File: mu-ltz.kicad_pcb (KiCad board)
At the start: 2 copper layers, 34.5 x 60 mm, 47 parts, among them J10 TRIM2, J2 GND, J3 Hi, J5 Lo, J6 Vin+, J9 TRIM1, Q1 MMBT3904LT1G, U1 LTZ1000, U2 AD8667, U3 ADA4523-1

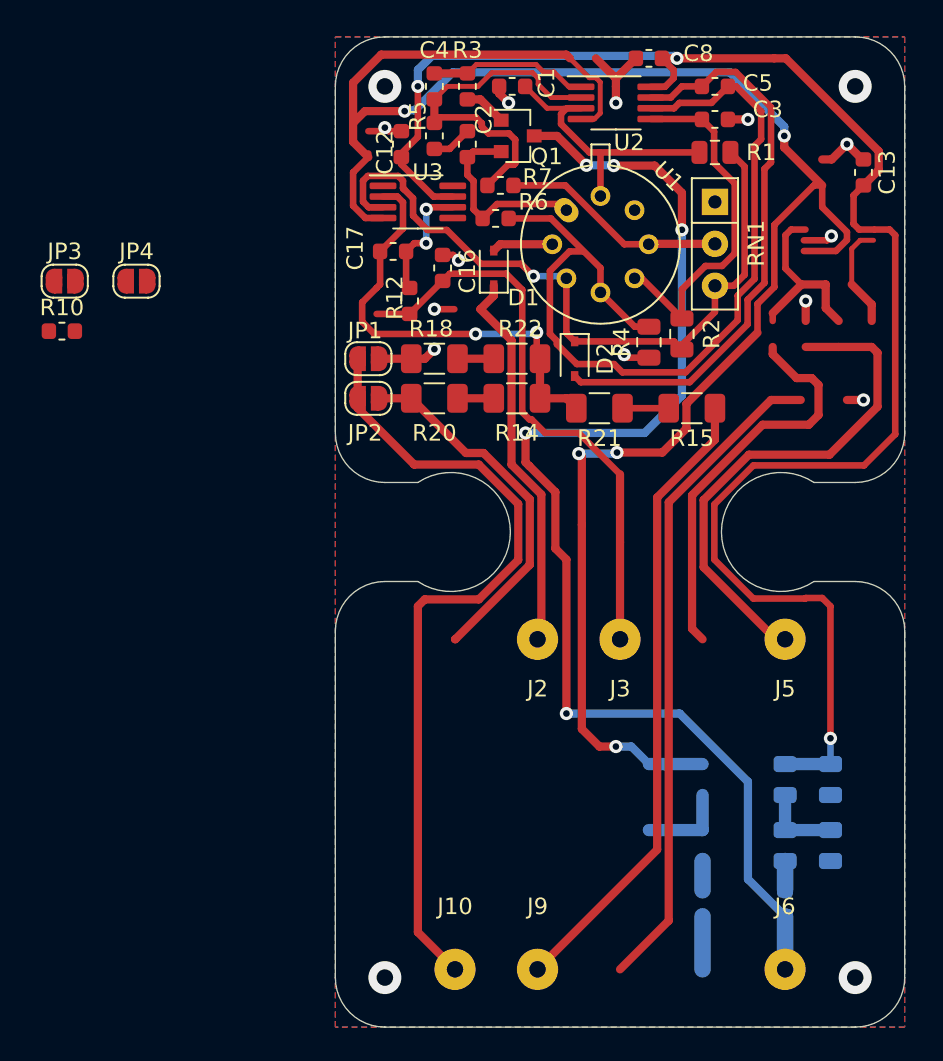
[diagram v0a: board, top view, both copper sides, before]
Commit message: Rev. 0.2 layout finished, not yet tested
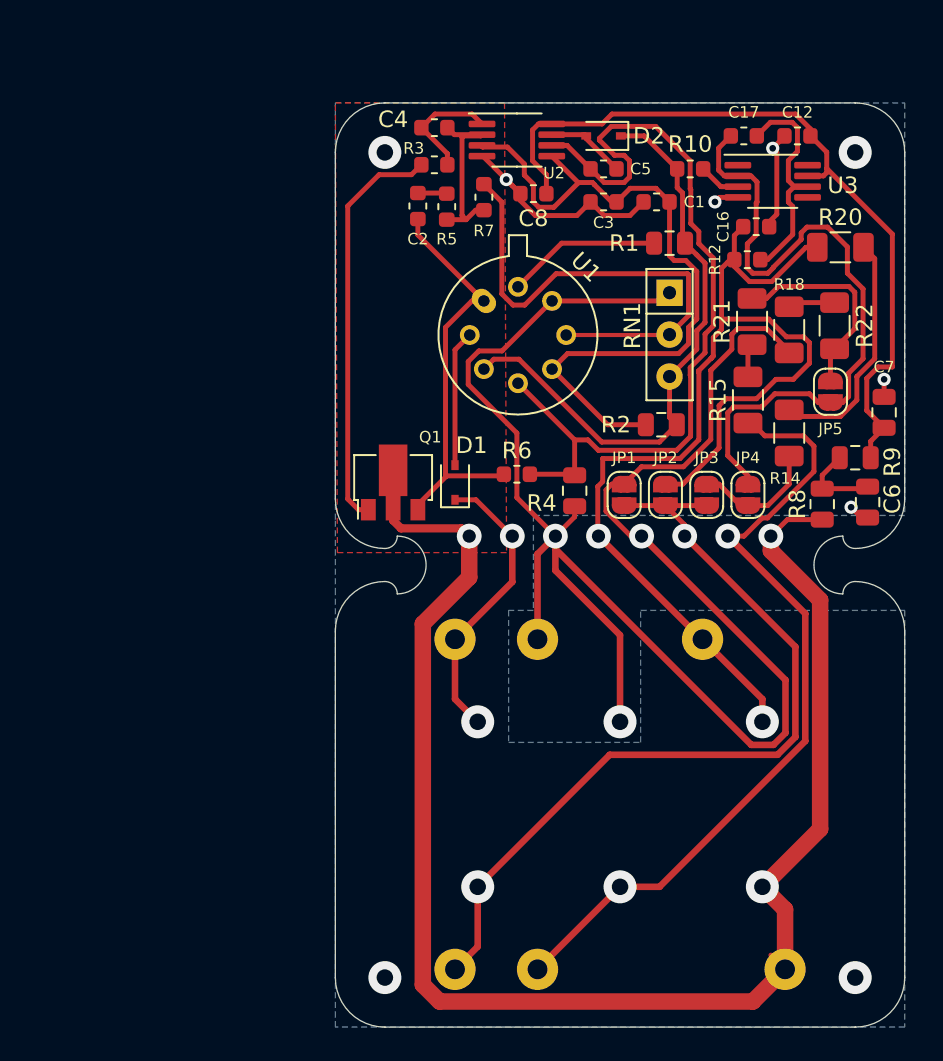
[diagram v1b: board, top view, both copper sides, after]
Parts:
- removed C13: 100nF, Capacitor_SMD:C_0603_1608Metric
- removed FB2: Ferrite_Bead_Small, Inductor_SMD:L_0603_1608Metric
- added JP3: Jumper_NO_Small, Jumper:SolderJumper-2_P1.3mm_Open_RoundedPad1.0x1.5mm, F.Cu at (122.5, 67.8)
- C6, C7, R8, R9: moved to F.Cu
- Q1: value MMBT3904LT1G -> 2SD1628G-TD-E; footprint Package_TO_SOT_SMD:SOT-23 -> Package_TO_SOT_SMD:SOT-89-3
- R6: value 400k -> dnp
- RN1: value 13k 1k -> 13k1k
- moved JP4 43.4 mm to (125.0, 67.8), turned to 270 degrees
- moved JP5 42.6 mm to (130.0, 61.5), turned to 90 degrees
- moved R10 39.3 mm to (121.5, 48.0), turned to 180 degrees
- moved R20 26.2 mm to (130.6, 52.8)
- moved C12 24.0 mm to (128.0, 46.0), turned to 0 degrees
- moved C7 22.5 mm to (133.2, 62.8), turned to 270 degrees
- moved C17 22.4 mm to (124.8, 46.0)
- moved Q1 22.3 mm to (103.5, 67.0), turned to 90 degrees
- moved R18 21.6 mm to (127.5, 57.8), turned to 90 degrees
- moved U3 21.5 mm to (126.5, 48.8)
- moved C6 20.9 mm to (132.2, 68.2)
- moved R8 20.8 mm to (129.5, 68.3)
- moved R12 20.6 mm to (125.0, 53.5), turned to 0 degrees
- moved R9 20.0 mm to (131.5, 65.5), turned to 180 degrees
- moved R22 19.4 mm to (130.2, 57.5), turned to 270 degrees
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- renumbered J2 to J1, J5 to J2, J3 to J4, JP3 to JP4, JP4 to JP5
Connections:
- D1 pad 1: Net-(D1-Pad1) -> /GND
- J1 pad 1: Net-(D1-Pad1) -> /GND
- J2 pad 1: Net-(D1-Pad1) -> /GND
- JP1 pad 1: Net-(D1-Pad1) -> /GND
- JP4 pad 2: Net-(J10-Pad1) -> Net-(JP3-Pad2)
- Q1 pad 2: Net-(C2-Pad2) -> /VCC
- Q1 pad 3: /VCC -> Net-(C2-Pad2)
- R14 pad 2: Net-(C17-Pad1) -> Net-(JP3-Pad2)
- R18 pad 1: Net-(D1-Pad1) -> /GND
- R4 pad 1: Net-(D1-Pad1) -> /GND
- R8 pad 2: Net-(FB2-Pad2) -> /VCC
- RN1 pad 1: Net-(D1-Pad1) -> /GND
- U1 pad 3: Net-(R10-Pad1) -> Net-(D2-Pad1)
- U1 pad 7: Net-(D1-Pad1) -> /GND
- U3 pad 3: Net-(D2-Pad1) -> Net-(R10-Pad1)
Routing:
- net Net-(D1-Pad1): track 60.4 -> 0.00 mm, vias 2 -> 0
- net /V+_filtered: track 101.2 -> 47.2 mm, vias 3 -> 0
- net Net-(J8-Pad1): track 40.1 -> 0.00 mm
- net Net-(C5-Pad2): track 34.6 -> 4.88 mm
- net Net-(J4-Pad1): track 24.5 -> 0.00 mm
- net Net-(Q1-Pad1): track 2.57 -> 25.0 mm
- net Net-(R7-Pad1): track 13.7 -> 29.9 mm
- net /VCC: track 76.1 -> 92.0 mm, vias 5 -> 3
- net Net-(C17-Pad1): track 27.1 -> 41.4 mm, vias 2 -> 0
- net Net-(C2-Pad2): track 11.9 -> 24.9 mm
- net Net-(JP5-Pad2): track 0.00 -> 12.7 mm
- net Net-(R14-Pad1): track 2.41 -> 14.8 mm
- net Net-(C18-Pad1): track 11.7 -> 0.00 mm
- net Net-(J9-Pad1): track 38.5 -> 49.4 mm, vias 0 -> 2
- net Net-(C16-Pad1): track 57.2 -> 67.9 mm, vias 0 -> 2
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- added copper zone on F.Cu, net /VCC
- removed copper zone on F.Cu, net /GND
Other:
- board size 34.5 x 60 mm -> 34.5 x 56 mm
- board text added: "---"
- board text added: "LTZmu 10DCV Standard reps June 2021"
- board text added: "This place is best shunned and left uninhabited."
- board text removed: "reps march 2021"
